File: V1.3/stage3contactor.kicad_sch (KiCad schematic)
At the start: 9 parts, among them J10 Screw_Terminal_01x02, J11 Screw_Terminal_01x02, J12 Screw_Terminal_01x02, J14 Screw_Terminal_01x02, J5 Screw_Terminal_01x02, J6 Screw_Terminal_01x02, J7 Screw_Terminal_01x02, J8 Screw_Terminal_01x02, J9 Screw_Terminal_01x02

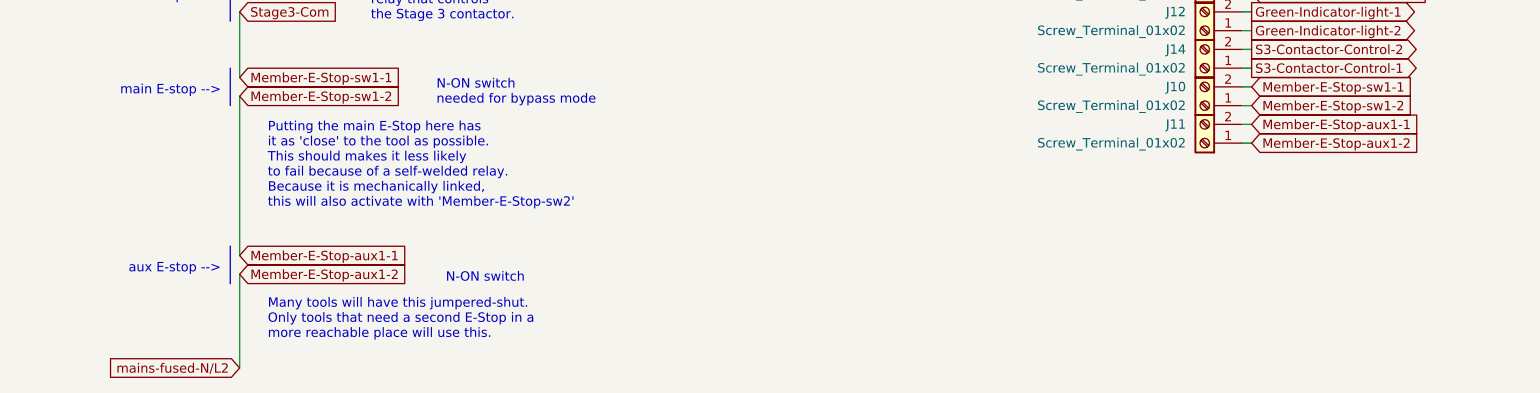
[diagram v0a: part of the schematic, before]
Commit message: rerouted to save space
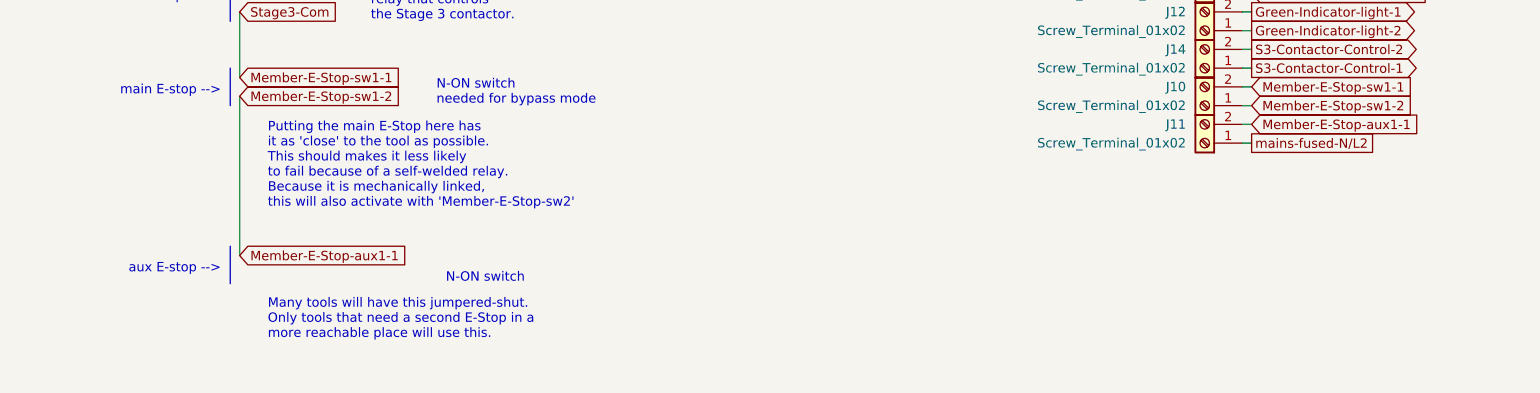
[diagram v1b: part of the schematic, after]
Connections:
- net Member-E-Stop-aux1-2 renamed mains-fused-N/L2
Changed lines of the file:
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@@
+    (stroke (width 0) (type default) (color 0 0 0 0))
+  )
+  (wire (pts (xy 201.93 137.16) (xy 203.2 137.16))
     (stroke (width 0) (type default) (color 0 0 0 0))
   )
@@
   )
   (wire (pts (xy 201.93 99.06) (xy 203.2 99.06))
-    (stroke (width 0) (type default) (color 0 0 0 0))
-  )
-  (wire (pts (xy 66.04 154.94) (xy 66.04 167.64))
-    (stroke (width 0) (type default) (color 0 0 0 0))
-  )
-  (wire (pts (xy 201.93 137.16) (xy 203.2 137.16))
     (stroke (width 0) (type default) (color 0 0 0 0))
   )
@@
     )
   )
-  (global_label "mains-fused-N{slash}L2" (shape input) (at 66.04 167.64 180) (fields_autoplaced)
-    (effects (font (size 1.27 1.27)) (justify right))
-    (property "Intersheet References" "${INTERSHEET_REFS}" (id 0) (at 44.8188 167.5606 0)
-      (effects (font (size 1.27 1.27)) (justify right) hide)
-    )
-  )
   (global_label "H{slash}L1" (shape passive) (at 203.2 96.52 0) (fields_autoplaced)
     (effects (font (size 1.27 1.27)) (justify left))
@@
     )
   )
+  (global_label "mains-fused-N{slash}L2" (shape passive) (at 203.2 137.16 0) (fields_autoplaced)
+    (effects (font (size 1.27 1.27)) (justify left))
+    (property "Intersheet References" "${INTERSHEET_REFS}" (id 0) (at 224.4212 137.0806 0)
+      (effects (font (size 1.27 1.27)) (justify left) hide)
+    )
+  )
   (global_label "Member-Red-Reset-Button-2" (shape input) (at 203.2 109.22 0) (fields_autoplaced)
     (effects (font (size 1.27 1.27)) (justify left))
@@
     )
   )
-  (global_label "Member-E-Stop-aux1-2" (shape input) (at 66.04 154.94 0) (fields_autoplaced)
-    (effects (font (size 1.27 1.27)) (justify left))
-    (property "Intersheet References" "${INTERSHEET_REFS}" (id 0) (at 93.1274 154.8606 0)
-      (effects (font (size 1.27 1.27)) (justify left) hide)
-    )
-  )
   (global_label "Member-E-Stop-aux1-1" (shape input) (at 203.2 134.62 0) (fields_autoplaced)
     (effects (font (size 1.27 1.27)) (justify left))
@@
       (effects (font (size 1.27 1.27)) (justify left) hide)
     )
-  )
-  (global_label "Member-E-Stop-aux1-2" (shape input) (at 203.2 137.16 0) (fields_autoplaced)
-    (effects (font (size 1.27 1.27)) (justify left))
-    (property "Intersheet References" "${INTERSHEET_REFS}" (id 0) (at 230.2874 137.0806 0)
-      (effects (font (size 1.27 1.27)) (justify left) hide)
-    )

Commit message: fixing edges and connecting all pieces
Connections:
- net Member-E-Stop-sw1-1: now also J11.1 (Pin_1); no longer J10.2 (Pin_2)
- net mains-fused-N/L2: now also J10.2 (Pin_2); no longer J11.1 (Pin_1)
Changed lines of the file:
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@@
   (junction (at 66.04 105.41) (diameter 0) (color 0 0 0 0)
   )
+  (wire (pts (xy 201.93 134.62) (xy 203.2 134.62))
+    (stroke (width 0) (type default) (color 0 0 0 0))
+  )
   (wire (pts (xy 66.04 101.6) (xy 66.04 105.41))
     (stroke (width 0) (type default) (color 0 0 0 0))
@@
     (stroke (width 0) (type default) (color 0 0 0 0))
   )
-  (wire (pts (xy 201.93 134.62) (xy 203.2 134.62))
-    (stroke (width 0) (type default) (color 0 0 0 0))
-  )
   (wire (pts (xy 66.04 105.41) (xy 66.04 115.57))
     (stroke (width 0) (type default) (color 0 0 0 0))
   )
+  (wire (pts (xy 66.04 95.25) (xy 100.33 95.25))
+    (stroke (width 0) (type default) (color 0 0 0 0))
+  )
+  (wire (pts (xy 66.04 130.81) (xy 66.04 152.4))
+    (stroke (width 0) (type default) (color 0 0 0 0))
+  )
+  (wire (pts (xy 201.93 127) (xy 203.2 127))
+    (stroke (width 0) (type default) (color 0 0 0 0))
+  )
+  (wire (pts (xy 201.93 96.52) (xy 203.2 96.52))
+    (stroke (width 0) (type default) (color 0 0 0 0))
+  )
+  (wire (pts (xy 201.93 109.22) (xy 203.2 109.22))
+    (stroke (width 0) (type default) (color 0 0 0 0))
+  )
+  (wire (pts (xy 66.04 105.41) (xy 100.33 105.41))
+    (stroke (width 0) (type default) (color 0 0 0 0))
+  )
+  (wire (pts (xy 201.93 114.3) (xy 203.2 114.3))
+    (stroke (width 0) (type default) (color 0 0 0 0))
+  )
+  (wire (pts (xy 201.93 93.98) (xy 203.2 93.98))
+    (stroke (width 0) (type default) (color 0 0 0 0))
+  )
+  (wire (pts (xy 66.04 95.25) (xy 66.04 99.06))
+    (stroke (width 0) (type default) (color 0 0 0 0))
+  )
+  (polyline (pts (xy 64.77 132.08) (xy 64.77 127))
+    (stroke (width 0) (type default) (color 0 0 0 0))
+  )
+  (wire (pts (xy 201.93 121.92) (xy 203.2 121.92))
+    (stroke (width 0) (type default) (color 0 0 0 0))
+  )
+  (polyline (pts (xy 64.77 151.13) (xy 64.77 156.21))
+    (stroke (width 0) (type default) (color 0 0 0 0))
+  )
+  (wire (pts (xy 66.04 119.38) (xy 66.04 128.27))
+    (stroke (width 0) (type default) (color 0 0 0 0))
+  )
+  (wire (pts (xy 201.93 104.14) (xy 203.2 104.14))
+    (stroke (width 0) (type default) (color 0 0 0 0))
+  )
+  (wire (pts (xy 201.93 101.6) (xy 203.2 101.6))
+    (stroke (width 0) (type default) (color 0 0 0 0))
+  )
+  (wire (pts (xy 66.04 90.17) (xy 66.04 95.25))
+    (stroke (width 0) (type default) (color 0 0 0 0))
+  )
+  (wire (pts (xy 201.93 99.06) (xy 203.2 99.06))
+    (stroke (width 0) (type default) (color 0 0 0 0))
+  )
+  (wire (pts (xy 201.93 132.08) (xy 203.2 132.08))
+    (stroke (width 0) (type default) (color 0 0 0 0))
+  )
+  (wire (pts (xy 201.93 106.68) (xy 203.2 106.68))
+    (stroke (width 0) (type default) (color 0 0 0 0))
+  )
   (wire (pts (xy 201.93 137.16) (xy 203.2 137.16))
     (stroke (width 0) (type default) (color 0 0 0 0))
   )
-  (wire (pts (xy 66.04 95.25) (xy 100.33 95.25))
-    (stroke (width 0) (type default) (color 0 0 0 0))
-  )
-  (wire (pts (xy 66.04 130.81) (xy 66.04 152.4))
-    (stroke (width 0) (type default) (color 0 0 0 0))
-  )
-  (wire (pts (xy 201.93 127) (xy 203.2 127))
-    (stroke (width 0) (type default) (color 0 0 0 0))
-  )
-  (wire (pts (xy 201.93 96.52) (xy 203.2 96.52))
-    (stroke (width 0) (type default) (color 0 0 0 0))
-  )
-  (wire (pts (xy 201.93 109.22) (xy 203.2 109.22))
-    (stroke (width 0) (type default) (color 0 0 0 0))
-  )
-  (wire (pts (xy 66.04 105.41) (xy 100.33 105.41))
-    (stroke (width 0) (type default) (color 0 0 0 0))
-  )
-  (wire (pts (xy 201.93 114.3) (xy 203.2 114.3))
-    (stroke (width 0) (type default) (color 0 0 0 0))
-  )
-  (wire (pts (xy 201.93 93.98) (xy 203.2 93.98))
-    (stroke (width 0) (type default) (color 0 0 0 0))
-  )
-  (wire (pts (xy 66.04 95.25) (xy 66.04 99.06))
-    (stroke (width 0) (type default) (color 0 0 0 0))
-  )
-  (wire (pts (xy 201.93 132.08) (xy 203.2 132.08))
-    (stroke (width 0) (type default) (color 0 0 0 0))
-  )
-  (polyline (pts (xy 64.77 132.08) (xy 64.77 127))
-    (stroke (width 0) (type default) (color 0 0 0 0))
-  )
-  (wire (pts (xy 201.93 121.92) (xy 203.2 121.92))
-    (stroke (width 0) (type default) (color 0 0 0 0))
-  )
-  (polyline (pts (xy 64.77 151.13) (xy 64.77 156.21))
-    (stroke (width 0) (type default) (color 0 0 0 0))
-  )
-  (wire (pts (xy 66.04 119.38) (xy 66.04 128.27))
-    (stroke (width 0) (type default) (color 0 0 0 0))
-  )
-  (wire (pts (xy 201.93 104.14) (xy 203.2 104.14))
-    (stroke (width 0) (type default) (color 0 0 0 0))
-  )
-  (wire (pts (xy 201.93 101.6) (xy 203.2 101.6))
-    (stroke (width 0) (type default) (color 0 0 0 0))
-  )
-  (wire (pts (xy 66.04 90.17) (xy 66.04 95.25))
-    (stroke (width 0) (type default) (color 0 0 0 0))
-  )
-  (wire (pts (xy 201.93 99.06) (xy 203.2 99.06))
-    (stroke (width 0) (type default) (color 0 0 0 0))
-  )
-  (wire (pts (xy 201.93 106.68) (xy 203.2 106.68))
+  (wire (pts (xy 201.93 119.38) (xy 203.2 119.38))
+    (stroke (width 0) (type default) (color 0 0 0 0))
+  )
+  (wire (pts (xy 201.93 124.46) (xy 203.2 124.46))
+    (stroke (width 0) (type default) (color 0 0 0 0))
+  )
+  (wire (pts (xy 201.93 116.84) (xy 203.2 116.84))
     (stroke (width 0) (type default) (color 0 0 0 0))
   )
   (wire (pts (xy 201.93 129.54) (xy 203.2 129.54))
-    (stroke (width 0) (type default) (color 0 0 0 0))
-  )
-  (wire (pts (xy 201.93 119.38) (xy 203.2 119.38))
-    (stroke (width 0) (type default) (color 0 0 0 0))
-  )
-  (wire (pts (xy 201.93 124.46) (xy 203.2 124.46))
-    (stroke (width 0) (type default) (color 0 0 0 0))
-  )
-  (wire (pts (xy 201.93 116.84) (xy 203.2 116.84))
     (stroke (width 0) (type default) (color 0 0 0 0))
   )
@@
     )
   )
-  (global_label "mains-fused-N{slash}L2" (shape passive) (at 203.2 137.16 0) (fields_autoplaced)
-    (effects (font (size 1.27 1.27)) (justify left))
-    (property "Intersheet References" "${INTERSHEET_REFS}" (id 0) (at 224.4212 137.0806 0)
+  (global_label "mains-fused-N{slash}L2" (shape passive) (at 203.2 129.54 0) (fields_autoplaced)
+    (effects (font (size 1.27 1.27)) (justify left))
+    (property "Intersheet References" "${INTERSHEET_REFS}" (id 0) (at 224.4212 129.4606 0)
       (effects (font (size 1.27 1.27)) (justify left) hide)
     )
@@
     )
   )
-  (global_label "Member-E-Stop-sw1-2" (shape input) (at 203.2 132.08 0) (fields_autoplaced)
-    (effects (font (size 1.27 1.27)) (justify left))
-    (property "Intersheet References" "${INTERSHEET_REFS}" (id 0) (at 229.3198 132.0006 0)
+  (global_label "Member-E-Stop-sw1-2" (shape input) (at 203.2 134.62 0) (fields_autoplaced)
+    (effects (font (size 1.27 1.27)) (justify left))
+    (property "Intersheet References" "${INTERSHEET_REFS}" (id 0) (at 229.3198 134.5406 0)
       (effects (font (size 1.27 1.27)) (justify left) hide)
     )
@@
     )
   )
-  (global_label "Member-E-Stop-aux1-1" (shape input) (at 203.2 134.62 0) (fields_autoplaced)
-    (effects (font (size 1.27 1.27)) (justify left))
-    (property "Intersheet References" "${INTERSHEET_REFS}" (id 0) (at 230.2874 134.5406 0)
+  (global_label "Member-E-Stop-aux1-1" (shape input) (at 203.2 132.08 0) (fields_autoplaced)
+    (effects (font (size 1.27 1.27)) (justify left))
+    (property "Intersheet References" "${INTERSHEET_REFS}" (id 0) (at 230.2874 132.0006 0)
       (effects (font (size 1.27 1.27)) (justify left) hide)
     )
@@
     )
   )
-  (global_label "Member-E-Stop-sw1-1" (shape input) (at 203.2 129.54 0) (fields_autoplaced)
-    (effects (font (size 1.27 1.27)) (justify left))
-    (property "Intersheet References" "${INTERSHEET_REFS}" (id 0) (at 229.3198 129.4606 0)
-      (effects (font (size 1.27 1.27)) (justify left) hide)
-    )
+  (global_label "Member-E-Stop-sw1-1" (shape input) (at 203.2 137.16 0) (fields_autoplaced)
+    (effects (font (size 1.27 1.27)) (justify left))
+    (property "Intersheet References" "${INTERSHEET_REFS}" (id 0) (at 229.3198 137.0806 0)
+      (effects (font (size 1.27 1.27)) (justify left) hide)
+    )

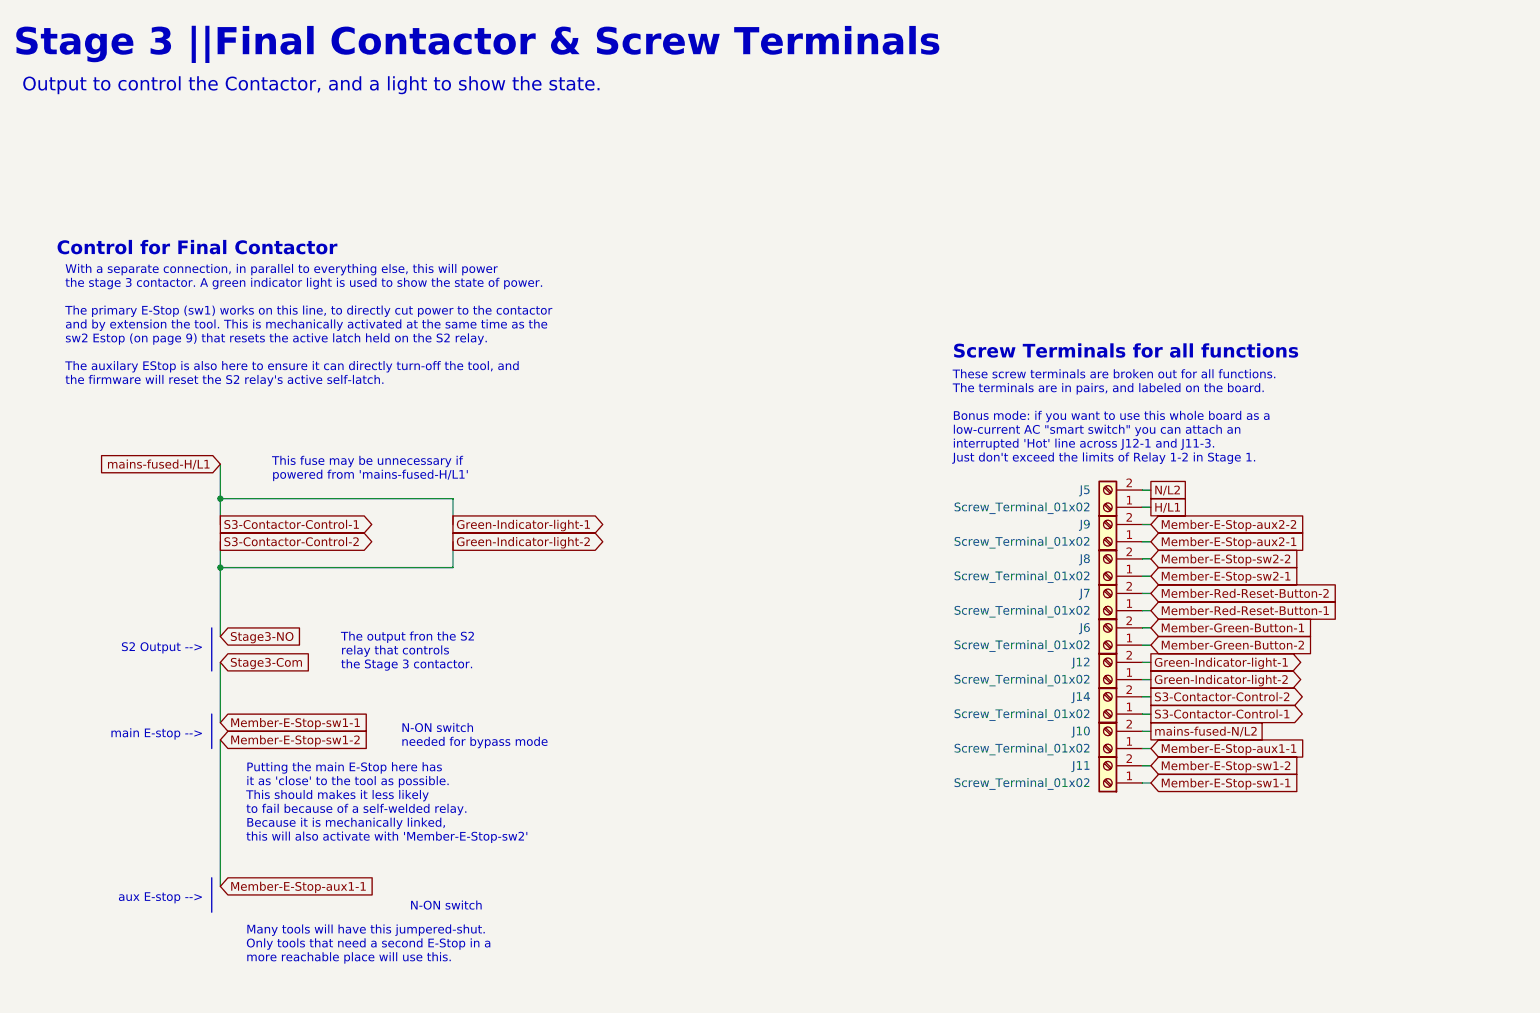
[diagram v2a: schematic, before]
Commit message: clarify door-activator role || Active & Passive door operation
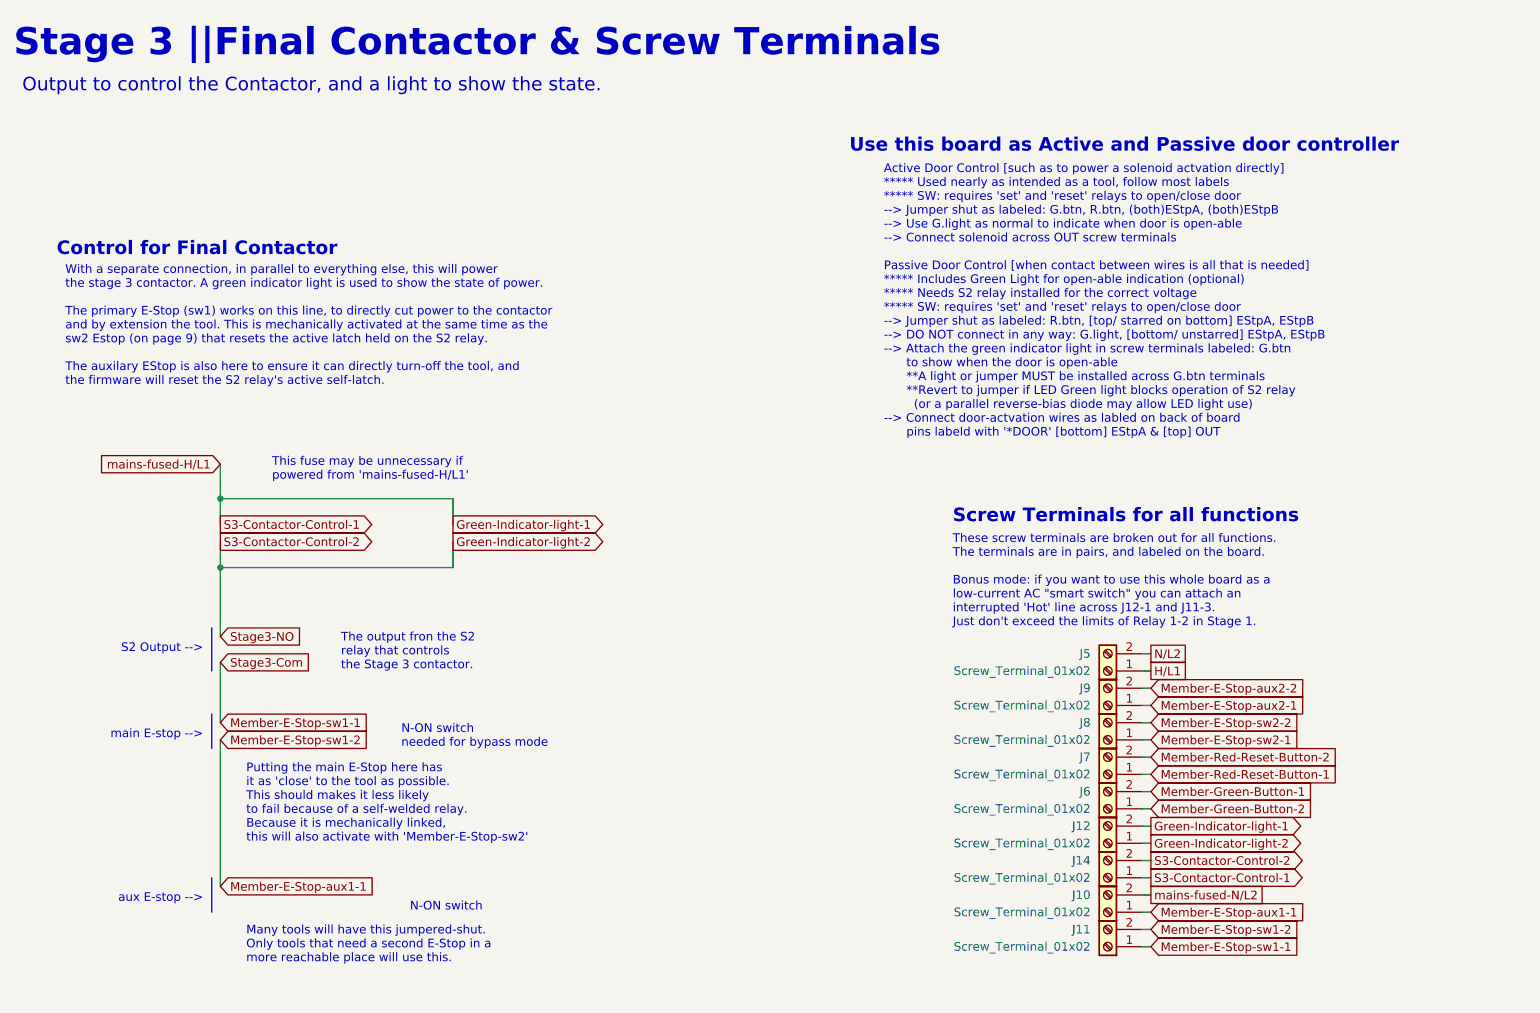
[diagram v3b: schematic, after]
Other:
- note added: "Active Door Control [such as to power a solenoid actvation directly] ***** Used nearly as intended as a tool, follow most labels ***** SW: requires 'set' and 'reset' relays to open/close door --> Jumper shut as labeled: G.btn, R.btn, (both)EStpA, (both)EStpB --> Use G.light as normal to indicate when door is open-able --> Connect solenoid across OUT screw terminals Passive Door Control [when cont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"
- note added: "Use this board as Active and Passive door controller"
- moved on the sheet: J10, J11, J12, J14, J5, J6, J7, J8, J9

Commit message: update v1.3 schematic documentation
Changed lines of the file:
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@@
   (text "Output to control the Contactor, and a light to show the state."
     (at 36.83 35.56 0)
-    (effects (font (size 2 2)) (justify left bottom))
+    (effects (font (size 2.5 2.5)) (justify left bottom))
   )
   (text "N-ON switch\nneeded for bypass mode" (at 92.71 132.08 0)

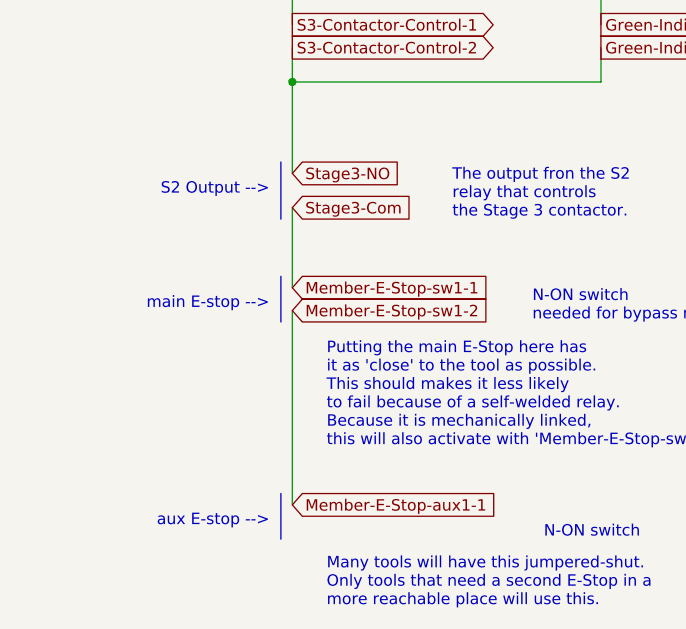
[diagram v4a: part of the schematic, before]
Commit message: started adding the feather footprint to the board. need to update board shape and silkscreens
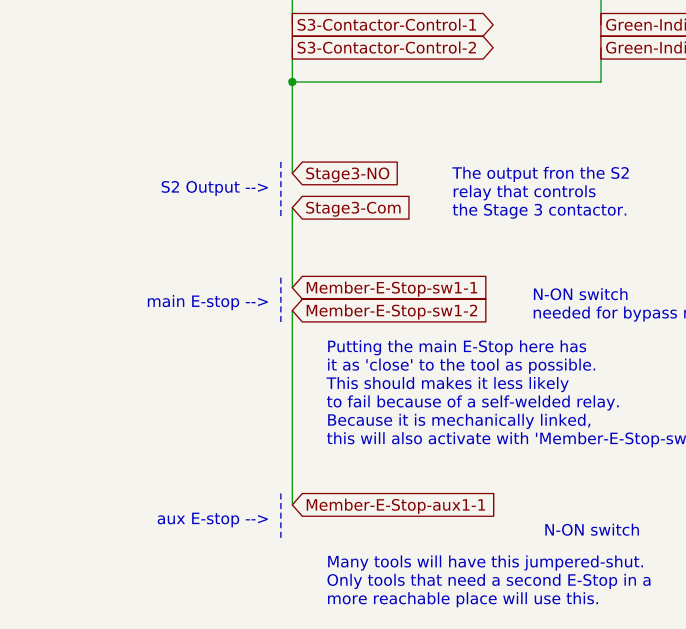
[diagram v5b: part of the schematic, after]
